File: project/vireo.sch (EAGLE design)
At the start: 4 parts, among them U1 STM32L476RG

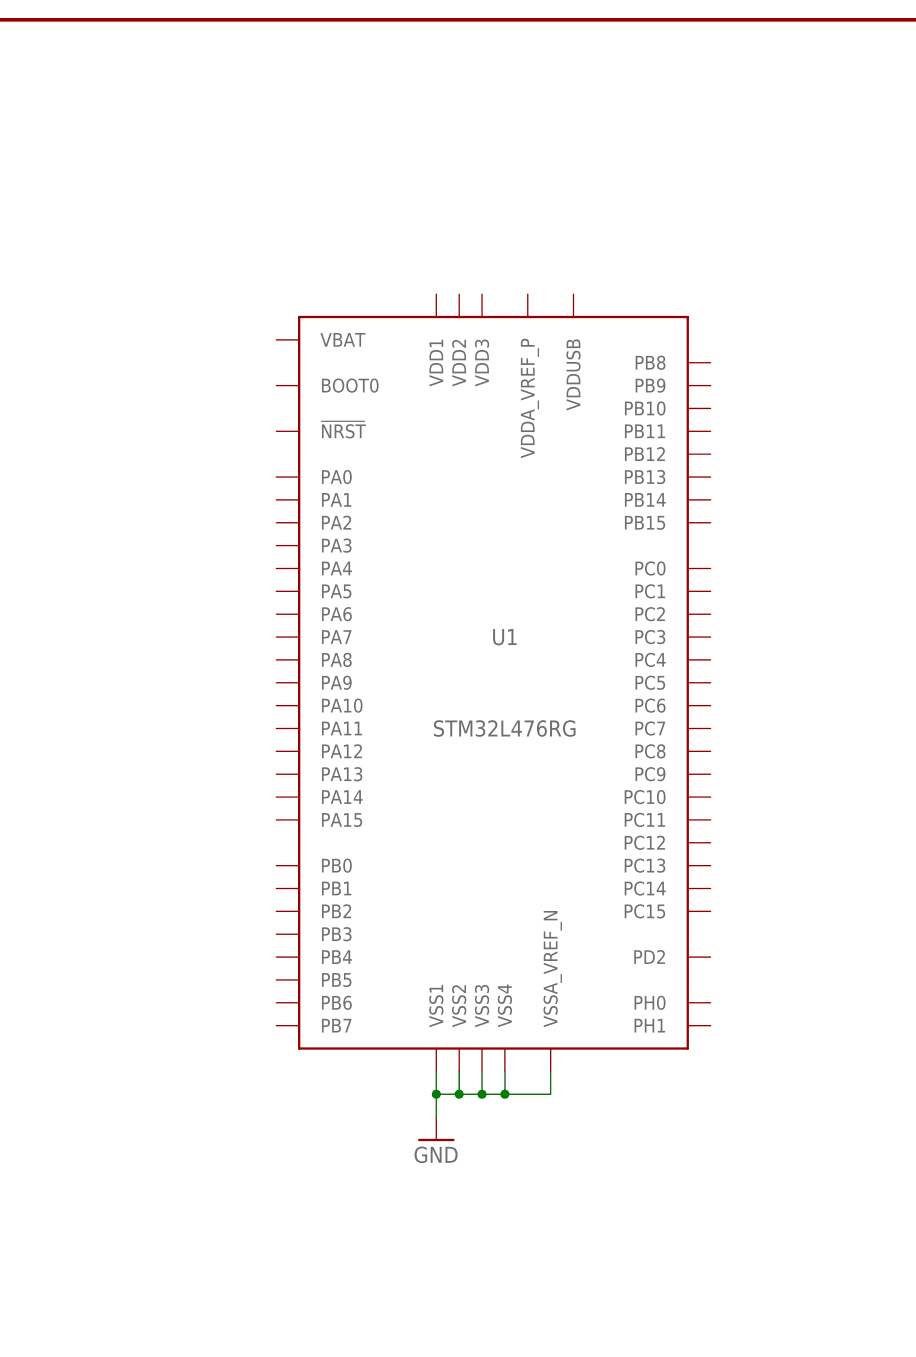
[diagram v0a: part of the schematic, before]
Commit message: Add VDD supply capacitor circuit for the L4
Signed-off-by: Greg Meiste <greg.meiste@gmail.com>
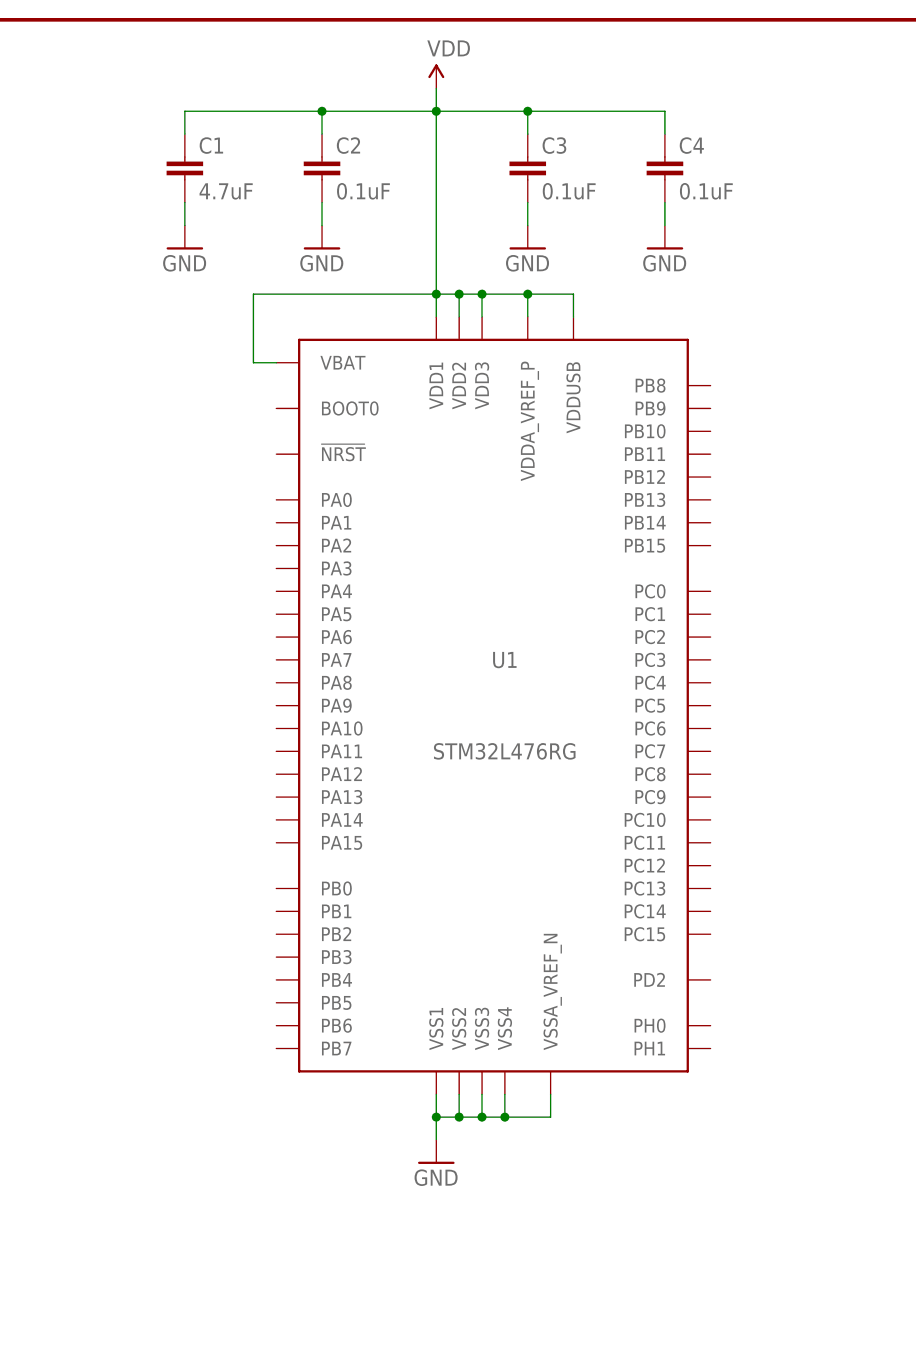
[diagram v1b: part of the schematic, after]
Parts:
- added C1: 4.7uF, SparkFun-Capacitors:CAP0603-CAP
- added C2, C3, C4: 0.1uF, SparkFun-Capacitors:CAP0603-CAP
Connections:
- net GND: now also C1.2, C2.2, C3.2, C4.2
- net VDD: now also C1.1, C2.1, C3.1, C4.1, U1.VBAT, U1.VDD1, U1.VDD2, U1.VDD3, U1.VDDA_VREF_P, U1.VDDUSB
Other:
- moved on the sheet: U1
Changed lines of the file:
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@@
 <part name="GND4" library="SparkFun-Aesthetics" deviceset="GND" device=""/>
 <part name="GND5" library="SparkFun-Aesthetics" deviceset="GND" device=""/>
+<part name="C1" library="SparkFun-Capacitors" deviceset="CAP" device="0603-CAP" value="4.7uF"/>
+<part name="C2" library="SparkFun-Capacitors" deviceset="CAP" device="0603-CAP" value="0.1uF"/>
+<part name="C3" library="SparkFun-Capacitors" deviceset="CAP" device="0603-CAP" value="0.1uF"/>
+<part name="C4" library="SparkFun-Capacitors" deviceset="CAP" device="0603-CAP" value="0.1uF"/>
+<part name="SUPPLY1" library="SparkFun-Aesthetics" deviceset="VDD" device=""/>
+<part name="GND6" library="SparkFun-Aesthetics" deviceset="GND" device=""/>
+<part name="GND7" library="SparkFun-Aesthetics" deviceset="GND" device=""/>
+<part name="GND8" library="SparkFun-Aesthetics" deviceset="GND" device=""/>
+<part name="GND9" library="SparkFun-Aesthetics" deviceset="GND" device=""/>
 </parts>
 <sheets>
@@
 <instance part="FRAME1" gate="G$1" x="0" y="0"/>
 <instance part="FRAME1" gate="V" x="147.32" y="0"/>
-<instance part="U1" gate="U1" x="129.54" y="111.76"/>
+<instance part="U1" gate="U1" x="129.54" y="109.22"/>
 <instance part="JP1" gate="G$1" x="238.76" y="134.62" rot="MR0"/>
 <instance part="JP2" gate="G$1" x="208.28" y="134.62" rot="MR0"/>
-<instance part="GND1" gate="1" x="121.92" y="60.96"/>
+<instance part="GND1" gate="1" x="121.92" y="58.42"/>
 <instance part="GND2" gate="1" x="218.44" y="93.98"/>
 <instance part="GND3" gate="1" x="187.96" y="93.98"/>
 <instance part="GND4" gate="1" x="185.42" y="170.18" rot="R270"/>
 <instance part="GND5" gate="1" x="215.9" y="170.18" rot="R270"/>
+<instance part="C1" gate="G$1" x="93.98" y="167.64"/>
+<instance part="C2" gate="G$1" x="109.22" y="167.64"/>
+<instance part="C3" gate="G$1" x="132.08" y="167.64"/>
+<instance part="C4" gate="G$1" x="147.32" y="167.64"/>
+<instance part="SUPPLY1" gate="VDD" x="121.92" y="177.8"/>
+<instance part="GND6" gate="1" x="93.98" y="160.02"/>
+<instance part="GND7" gate="1" x="109.22" y="160.02"/>
+<instance part="GND8" gate="1" x="132.08" y="160.02"/>
+<instance part="GND9" gate="1" x="147.32" y="160.02"/>
 </instances>
 <busses>
@@
 <pinref part="U1" gate="U1" pin="VSS1"/>
 <pinref part="GND1" gate="1" pin="GND"/>
-<wire x1="121.92" y1="68.58" x2="121.92" y2="66.04" width="0.1524" layer="91"/>
+<wire x1="121.92" y1="66.04" x2="121.92" y2="63.5" width="0.1524" layer="91"/>
 <pinref part="U1" gate="U1" pin="VSS2"/>
-<wire x1="121.92" y1="66.04" x2="121.92" y2="63.5" width="0.1524" layer="91"/>
-<wire x1="124.46" y1="68.58" x2="124.46" y2="66.04" width="0.1524" layer="91"/>
-<wire x1="124.46" y1="66.04" x2="121.92" y2="66.04" width="0.1524" layer="91"/>
-<junction x="121.92" y="66.04"/>
+<wire x1="121.92" y1="63.5" x2="121.92" y2="60.96" width="0.1524" layer="91"/>
+<wire x1="124.46" y1="66.04" x2="124.46" y2="63.5" width="0.1524" layer="91"/>
+<wire x1="124.46" y1="63.5" x2="121.92" y2="63.5" width="0.1524" layer="91"/>
+<junction x="121.92" y="63.5"/>
 <pinref part="U1" gate="U1" pin="VSS3"/>
-<wire x1="127" y1="68.58" x2="127" y2="66.04" width="0.1524" layer="91"/>
-<wire x1="127" y1="66.04" x2="124.46" y2="66.04" width="0.1524" layer="91"/>
-<junction x="124.46" y="66.04"/>
+<wire x1="127" y1="66.04" x2="127" y2="63.5" width="0.1524" layer="91"/>
+<wire x1="127" y1="63.5" x2="124.46" y2="63.5" width="0.1524" layer="91"/>
+<junction x="124.46" y="63.5"/>
 <pinref part="U1" gate="U1" pin="VSS4"/>
-<wire x1="129.54" y1="68.58" x2="129.54" y2="66.04" width="0.1524" layer="91"/>
-<wire x1="129.54" y1="66.04" x2="127" y2="66.04" width="0.1524" layer="91"/>
-<junction x="127" y="66.04"/>
+<wire x1="129.54" y1="66.04" x2="129.54" y2="63.5" width="0.1524" layer="91"/>
+<wire x1="129.54" y1="63.5" x2="127" y2="63.5" width="0.1524" layer="91"/>
+<junction x="127" y="63.5"/>
 <pinref part="U1" gate="U1" pin="VSSA_VREF_N"/>
-<wire x1="134.62" y1="68.58" x2="134.62" y2="66.04" width="0.1524" layer="91"/>
-<wire x1="134.62" y1="66.04" x2="129.54" y2="66.04" width="0.1524" layer="91"/>
-<junction x="129.54" y="66.04"/>
+<wire x1="134.62" y1="66.04" x2="134.62" y2="63.5" width="0.1524" layer="91"/>
+<wire x1="134.62" y1="63.5" x2="129.54" y2="63.5" width="0.1524" layer="91"/>
+<junction x="129.54" y="63.5"/>
 </segment>
 <segment>
@@
 <wire x1="200.66" y1="170.18" x2="187.96" y2="170.18" width="0.1524" layer="91"/>
 </segment>
+<segment>
+<pinref part="C1" gate="G$1" pin="2"/>
+<pinref part="GND6" gate="1" pin="GND"/>
+<wire x1="93.98" y1="165.1" x2="93.98" y2="162.56" width="0.1524" layer="91"/>
+</segment>
+<segment>
+<pinref part="C2" gate="G$1" pin="2"/>
+<pinref part="GND7" gate="1" pin="GND"/>
+<wire x1="109.22" y1="165.1" x2="109.22" y2="162.56" width="0.1524" layer="91"/>
+</segment>
+<segment>
+<pinref part="C3" gate="G$1" pin="2"/>
+<pinref part="GND8" gate="1" pin="GND"/>
+<wire x1="132.08" y1="165.1" x2="132.08" y2="162.56" width="0.1524" layer="91"/>
+</segment>
+<segment>
+<pinref part="C4" gate="G$1" pin="2"/>
+<pinref part="GND9" gate="1" pin="GND"/>
+<wire x1="147.32" y1="165.1" x2="147.32" y2="162.56" width="0.1524" layer="91"/>
+</segment>
 </net>
 <net name="PA3" class="0">
@@
 <label x="218.44" y="162.56" size="2.54" layer="95"/>
 </segment>
-</net>
+<segment>
+<pinref part="U1" gate="U1" pin="VDD1"/>
+<wire x1="121.92" y1="152.4" x2="121.92" y2="154.94" width="0.1524" layer="91"/>
+<pinref part="U1" gate="U1" pin="VBAT"/>
+<wire x1="104.14" y1="147.32" x2="101.6" y2="147.32" width="0.1524" layer="91"/>
+<wire x1="101.6" y1="147.32" x2="101.6" y2="154.94" width="0.1524" layer="91"/>
+<wire x1="101.6" y1="154.94" x2="121.92" y2="154.94" width="0.1524" layer="91"/>
+<junction x="121.92" y="154.94"/>
+<pinref part="U1" gate="U1" pin="VDD2"/>
+<wire x1="124.46" y1="152.4" x2="124.46" y2="154.94" width="0.1524" layer="91"/>
+<wire x1="124.46" y1="154.94" x2="121.92" y2="154.94" width="0.1524" layer="91"/>
+<pinref part="U1" gate="U1" pin="VDD3"/>
+<wire x1="124.46" y1="154.94" x2="127" y2="154.94" width="0.1524" layer="91"/>
+<wire x1="127" y1="154.94" x2="127" y2="152.4" width="0.1524" layer="91"/>
+<junction x="124.46" y="154.94"/>
+<pinref part="U1" gate="U1" pin="VDDA_VREF_P"/>
+<wire x1="127" y1="154.94" x2="132.08" y2="154.94" width="0.1524" layer="91"/>
+<wire x1="132.08" y1="154.94" x2="132.08" y2="152.4" width="0.1524" layer="91"/>
+<junction x="127" y="154.94"/>
+<pinref part="U1" gate="U1" pin="VDDUSB"/>
+<wire x1="132.08" y1="154.94" x2="137.16" y2="154.94" width="0.1524" layer="91"/>
+<wire x1="137.16" y1="154.94" x2="137.16" y2="152.4" width="0.1524" layer="91"/>
+<junction x="132.08" y="154.94"/>
+<pinref part="SUPPLY1" gate="VDD" pin="VDD"/>
+<wire x1="121.92" y1="177.8" x2="121.92" y2="175.26" width="0.1524" layer="91"/>
+<pinref part="C2" gate="G$1" pin="1"/>
+<wire x1="121.92" y1="175.26" x2="121.92" y2="154.94" width="0.1524" layer="91"/>
+<wire x1="109.22" y1="172.72" x2="109.22" y2="175.26" width="0.1524" layer="91"/>
+<wire x1="109.22" y1="175.26" x2="121.92" y2="175.26" width="0.1524" layer="91"/>
+<junction x="121.92" y="175.26"/>
+<pinref part="C1" gate="G$1" pin="1"/>
+<wire x1="109.22" y1="175.26" x2="93.98" y2="175.26" width="0.1524" layer="91"/>
+<wire x1="93.98" y1="175.26" x2="93.98" y2="172.72" width="0.1524" layer="91"/>
+<junction x="109.22" y="175.26"/>
+<pinref part="C3" gate="G$1" pin="1"/>
+<wire x1="121.92" y1="175.26" x2="132.08" y2="175.26" width="0.1524" layer="91"/>
+<wire x1="132.08" y1="175.26" x2="132.08" y2="172.72" width="0.1524" layer="91"/>
+<pinref part="C4" gate="G$1" pin="1"/>
+<wire x1="132.08" y1="175.26" x2="147.32" y2="175.26" width="0.1524" layer="91"/>
+<wire x1="147.32" y1="175.26" x2="147.32" y2="172.72" width="0.1524" layer="91"/>
+<junction x="132.08" y="175.26"/>
+</segment>
+</net>

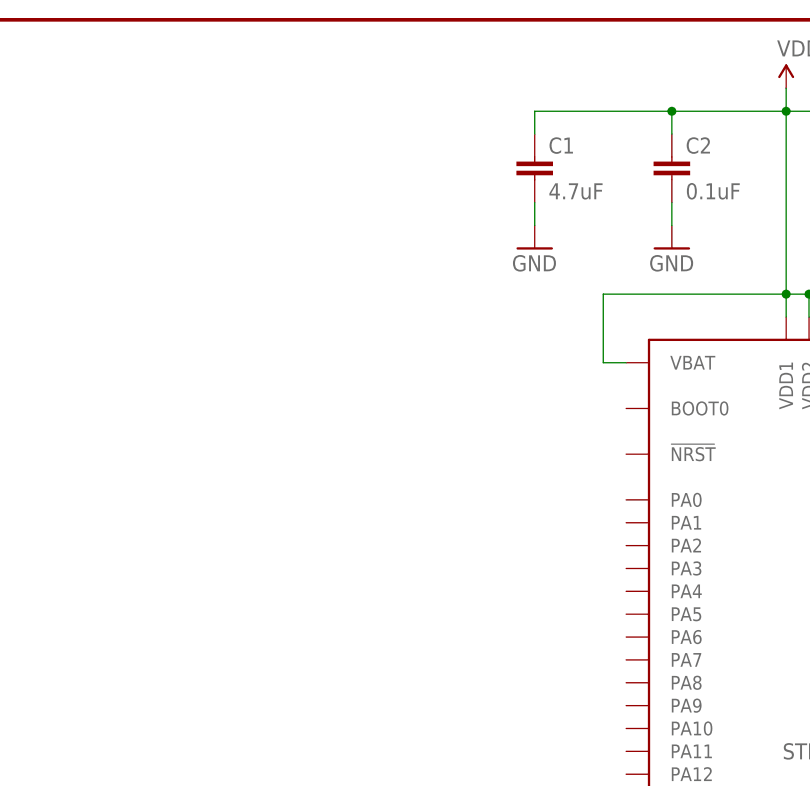
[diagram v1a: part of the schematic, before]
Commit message: Add BOOT0 and NRST circuits
Signed-off-by: Greg Meiste <greg.meiste@gmail.com>
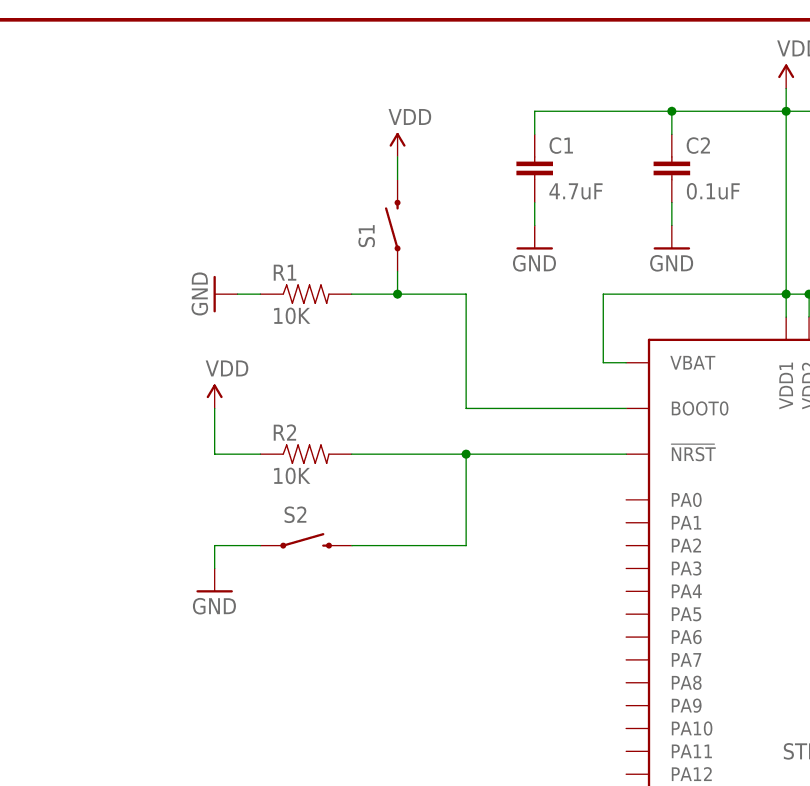
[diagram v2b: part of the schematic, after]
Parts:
- added R1, R2: 10K, SparkFun-Passives:RESISTOR0603-RES
- added S1, S2: SWITCH-MOMENTARY-2SMD-3, SparkFun-Electromechanical:SWITCH-MOMENTARY-2SMD-3
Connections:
- net BOOT0: now also R1.2, S1.1, U1.BOOT0
- net GND: now also R1.1, S2.1
- net NRST: now also R2.2, S2.2, U1.!NRST
- net VDD: now also R2.1, S1.2
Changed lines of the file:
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@@
 <part name="GND8" library="SparkFun-Aesthetics" deviceset="GND" device=""/>
 <part name="GND9" library="SparkFun-Aesthetics" deviceset="GND" device=""/>
+<part name="S1" library="SparkFun-Electromechanical" deviceset="SWITCH-MOMENTARY-2" device="SMD-3" value=""/>
+<part name="R1" library="SparkFun-Passives" deviceset="RESISTOR" device="0603-RES" value="10K"/>
+<part name="GND10" library="SparkFun-Aesthetics" deviceset="GND" device=""/>
+<part name="SUPPLY2" library="SparkFun-Aesthetics" deviceset="VDD" device=""/>
+<part name="SUPPLY3" library="SparkFun-Aesthetics" deviceset="VDD" device=""/>
+<part name="GND11" library="SparkFun-Aesthetics" deviceset="GND" device=""/>
+<part name="R2" library="SparkFun-Passives" deviceset="RESISTOR" device="0603-RES" value="10K"/>
+<part name="S2" library="SparkFun-Electromechanical" deviceset="SWITCH-MOMENTARY-2" device="SMD-3" value=""/>
 </parts>
 <sheets>
@@
 <instance part="GND8" gate="1" x="132.08" y="160.02"/>
 <instance part="GND9" gate="1" x="147.32" y="160.02"/>
+<instance part="S1" gate="G$1" x="78.74" y="162.56" rot="R90"/>
+<instance part="R1" gate="G$1" x="68.58" y="154.94"/>
+<instance part="GND10" gate="1" x="58.42" y="154.94" rot="R270"/>
+<instance part="SUPPLY2" gate="VDD" x="78.74" y="170.18"/>
+<instance part="SUPPLY3" gate="VDD" x="58.42" y="142.24"/>
+<instance part="GND11" gate="1" x="58.42" y="121.92"/>
+<instance part="R2" gate="G$1" x="68.58" y="137.16"/>
+<instance part="S2" gate="G$1" x="68.58" y="127"/>
 </instances>
 <busses>
@@
 <pinref part="GND9" gate="1" pin="GND"/>
 <wire x1="147.32" y1="165.1" x2="147.32" y2="162.56" width="0.1524" layer="91"/>
+</segment>
+<segment>
+<pinref part="R1" gate="G$1" pin="1"/>
+<pinref part="GND10" gate="1" pin="GND"/>
+<wire x1="63.5" y1="154.94" x2="60.96" y2="154.94" width="0.1524" layer="91"/>
+</segment>
+<segment>
+<pinref part="S2" gate="G$1" pin="1"/>
+<pinref part="GND11" gate="1" pin="GND"/>
+<wire x1="63.5" y1="127" x2="58.42" y2="127" width="0.1524" layer="91"/>
+<wire x1="58.42" y1="127" x2="58.42" y2="124.46" width="0.1524" layer="91"/>
 </segment>
 </net>
@@
 <junction x="132.08" y="175.26"/>
 </segment>
+<segment>
+<pinref part="SUPPLY2" gate="VDD" pin="VDD"/>
+<pinref part="S1" gate="G$1" pin="2"/>
+<wire x1="78.74" y1="170.18" x2="78.74" y2="167.64" width="0.1524" layer="91"/>
+</segment>
+<segment>
+<pinref part="R2" gate="G$1" pin="1"/>
+<pinref part="SUPPLY3" gate="VDD" pin="VDD"/>
+<wire x1="63.5" y1="137.16" x2="58.42" y2="137.16" width="0.1524" layer="91"/>
+<wire x1="58.42" y1="137.16" x2="58.42" y2="142.24" width="0.1524" layer="91"/>
+</segment>
 </net>
 <net name="PA2" class="0">
@@
 <label x="187.96" y="119.38" size="2.54" layer="95"/>
 </segment>
+<segment>
+<pinref part="U1" gate="U1" pin="!NRST"/>
+<pinref part="R2" gate="G$1" pin="2"/>
+<wire x1="104.14" y1="137.16" x2="86.36" y2="137.16" width="0.1524" layer="91"/>
+<pinref part="S2" gate="G$1" pin="2"/>
+<wire x1="86.36" y1="137.16" x2="73.66" y2="137.16" width="0.1524" layer="91"/>
+<wire x1="73.66" y1="127" x2="86.36" y2="127" width="0.1524" layer="91"/>
+<wire x1="86.36" y1="127" x2="86.36" y2="137.16" width="0.1524" layer="91"/>
+<junction x="86.36" y="137.16"/>
+</segment>
 </net>
 <net name="PH1" class="0">
@@
 <label x="187.96" y="139.7" size="2.54" layer="95"/>
 </segment>
-</net>
+<segment>
+<pinref part="R1" gate="G$1" pin="2"/>
+<pinref part="S1" gate="G$1" pin="1"/>
+<wire x1="78.74" y1="154.94" x2="73.66" y2="154.94" width="0.1524" layer="91"/>
+<wire x1="78.74" y1="157.48" x2="78.74" y2="154.94" width="0.1524" layer="91"/>
+<wire x1="78.74" y1="154.94" x2="86.36" y2="154.94" width="0.1524" layer="91"/>
+<wire x1="86.36" y1="154.94" x2="86.36" y2="142.24" width="0.1524" layer="91"/>
+<junction x="78.74" y="154.94"/>
+<pinref part="U1" gate="U1" pin="BOOT0"/>
+<wire x1="86.36" y1="142.24" x2="104.14" y2="142.24" width="0.1524" layer="91"/>
+</segment>
+</net>
